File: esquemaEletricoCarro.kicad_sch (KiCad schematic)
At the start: 25 parts, among them M1 Motor_DC, M2 Motor_DC, M3 Motor_Servo, SW1 Botão emergência, U1 Motor_driver_43a_Bts7960b, U2 Motor_driver_43a_Bts7960b, U3 HC-Sr04, U4 HC-Sr04, U5 HC-Sr04, U6 KY-040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

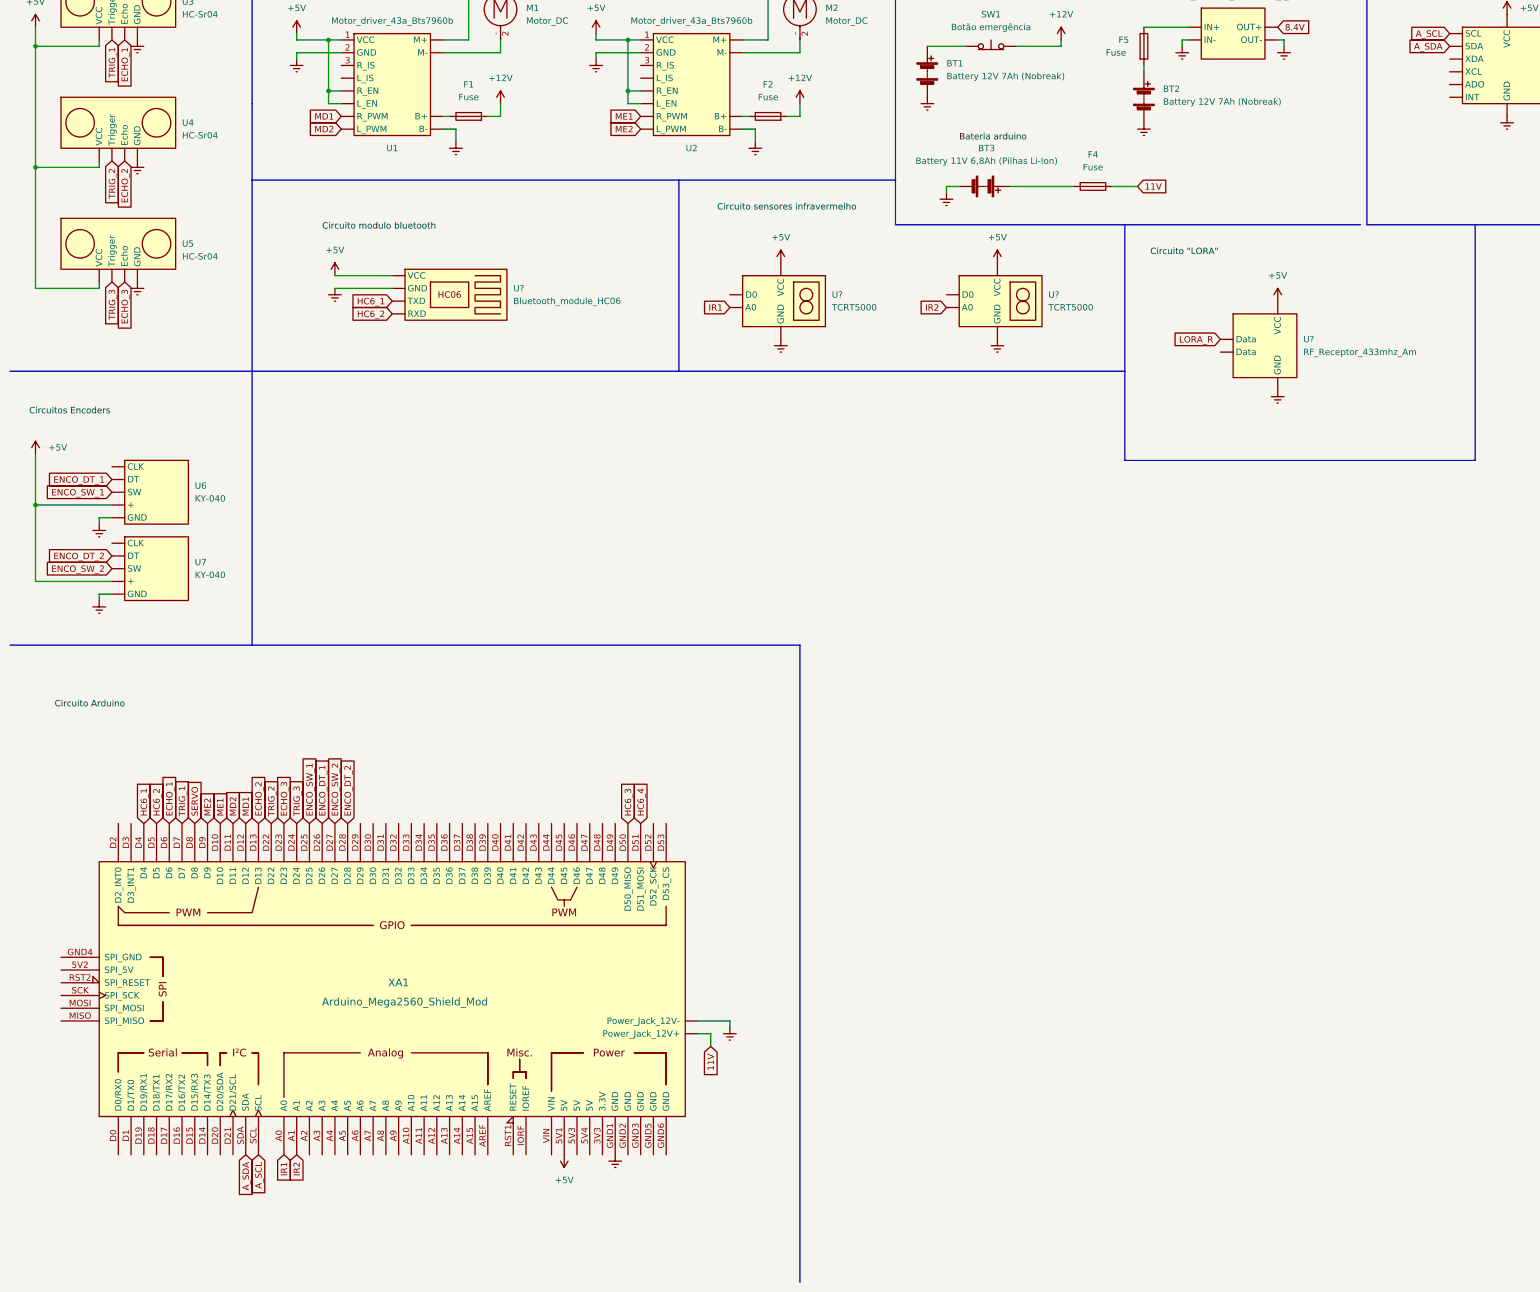
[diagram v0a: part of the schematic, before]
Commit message: fix: alteração nos pinos do arduino
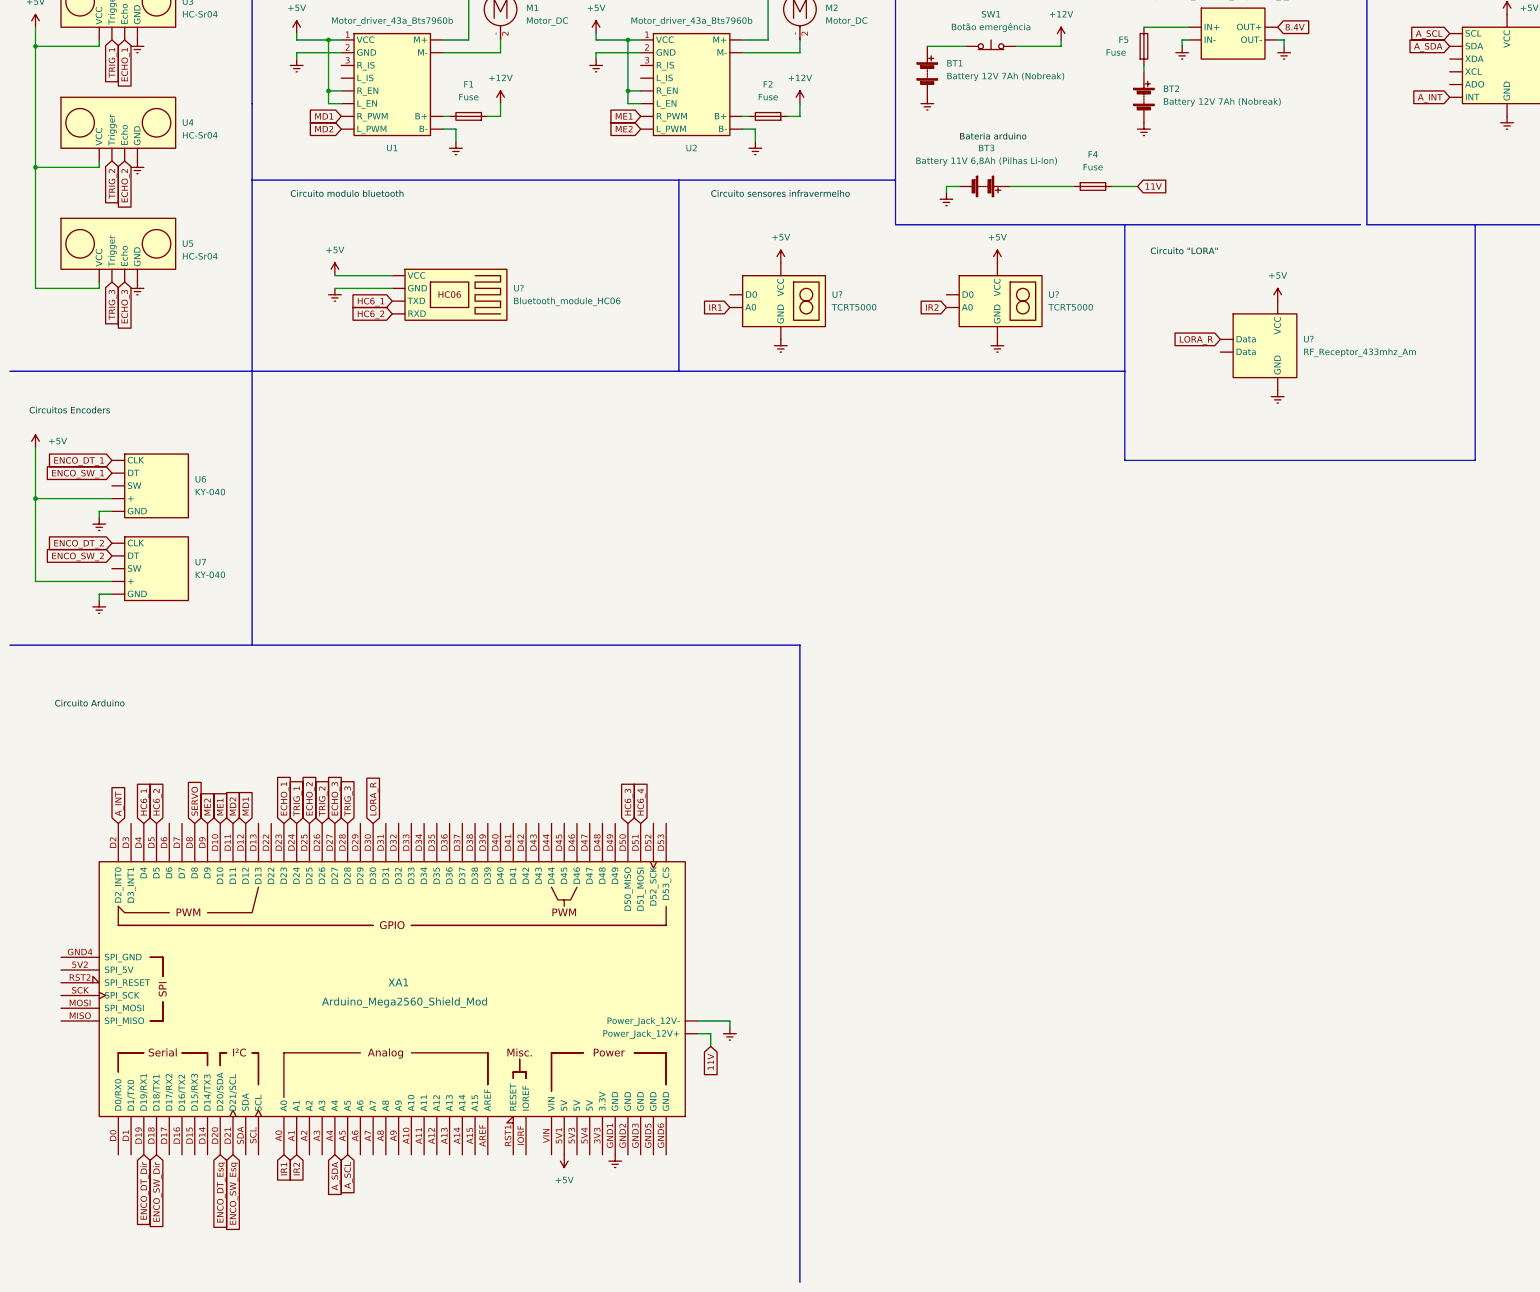
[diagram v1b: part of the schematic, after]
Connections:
- net A_SCL: now also XA1.A5; no longer XA1.SCL
- net A_SDA: now also XA1.A4; no longer XA1.SDA
- net ECHO_1: now also XA1.D23; no longer XA1.D6
- net ECHO_2: now also XA1.D25; no longer XA1.D13
- net ECHO_3: now also XA1.D27; no longer XA1.D23
- net ENCO_DT_1: no longer XA1.D26
- net ENCO_DT_2: no longer XA1.D28
- net ENCO_SW_1: no longer XA1.D25
- net ENCO_SW_2: no longer XA1.D27
- net LORA_R: now also XA1.D30
- net TRIG_1: now also XA1.D24; no longer XA1.D7
- net TRIG_2: now also XA1.D26; no longer XA1.D22
- net TRIG_3: now also XA1.D28; no longer XA1.D24
- net ENCO_SW_Dir: now reaches XA1.D18 (D18/TX1)
- net ENCO_DT_Dir: now reaches XA1.D19 (D19/RX1)
- net A_INT: now reaches XA1.D2 (D2_INT0)
- net A_INT: now also U?. (XDA)
- net ENCO_DT_Esq: now reaches XA1.D20 (D20/SDA)
- net ENCO_SW_Esq: now reaches XA1.D21 (D21/SCL)
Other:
- moved on the sheet: U6

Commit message: feat: reorganizacao e adicao de novos circuitos
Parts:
- removed BT1, BT2: Battery 12V 7Ah (Nobreak), symbol Device:Battery
- removed BT3: Battery 11V 6,8Ah (Pilhas Li-Ion), symbol Device:Battery
- removed F1, F2, F4, F5: Fuse, symbol Device:Fuse
- removed M1, M2: Motor_DC, symbol Motor:Motor_DC
- removed M3: Motor_Servo, symbol Motor:Motor_Servo
- removed SW1: Botão emergência, symbol Switch:SW_Push_Open
- removed U1, U2: Motor_driver_43a_Bts7960b, symbol Customizados:Motor_driver_43a_Bts7960b
- removed U3, U4, U5: HC-Sr04, symbol Customizados:HC-Sr04
- removed U6, U7: KY-040, symbol Customizados:KY-040
- removed U?: MPU-6050_module, symbol Customizados:MPU-6050_module
- removed U?: Adjustable_Tension_Regulator_-_XL4015, symbol Customizados:Adjustable_Tension_Regulator_-_XL4015
- removed U?: Bluetooth_module_HC06, symbol Customizados:Bluetooth_module_HC06
- removed U?: RF_Receptor_433mhz_Am, symbol Customizados:RF_Receptor_433mhz_Am
- removed U? (x2): TCRT5000, symbol Customizados:TCRT5000
- removed XA1: Arduino_Mega2560_Shield_Mod, PCM_arduino-library:Arduino_Mega2560_Shield, symbol PCM_arduino-library:Arduino_Mega2560_Shield_Mod
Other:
- added sheet Alimentacao (alimentacao.kicad_sch)
- added sheet Arduino (arduino.kicad_sch)
- added sheet Motoroes (motores.kicad_sch)
- added sheet Outros (outros.kicad_sch)
- added sheet Sensores (sensores.kicad_sch)
- note removed: "Motor Esquerdo"
- note removed: "Motor direito"
